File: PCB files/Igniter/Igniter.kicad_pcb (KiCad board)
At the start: 2 copper layers, 154.5 x 119.6 mm, 53 parts, among them IC1 74HC4050, J1 Micro_SD_Card, J2 Battery, J3 PT2, J4 PT1, J5 PT3, J6 PT4, J7 IgnitionCoil, Q1 N MOSFET, Q2 N MOSFET, Q3 N MOSFET, Q4 N MOSFET, Q5 N MOSFET, Q6 N MOSFET, U1 MIC3490, U2 FDS8984, U3 FDS8984, U4 FDS8984

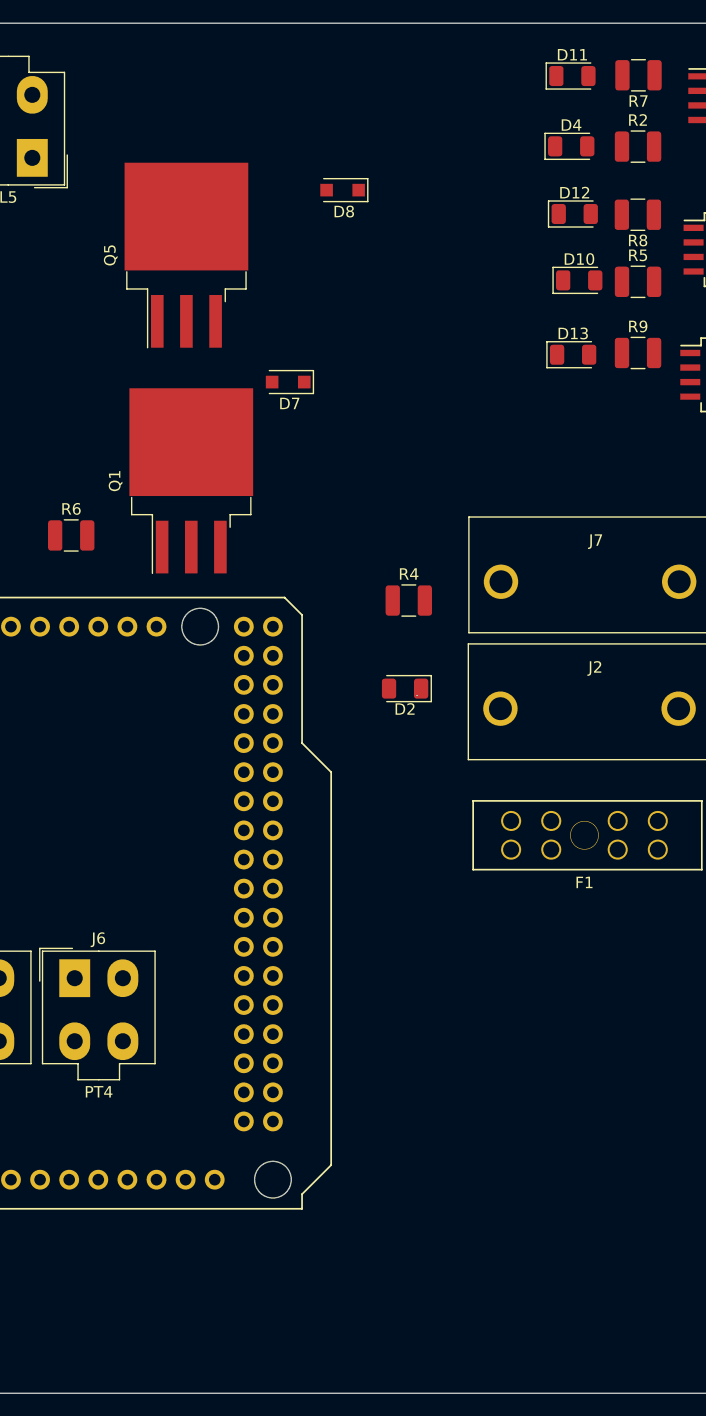
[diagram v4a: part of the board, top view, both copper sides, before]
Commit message: 11/14/2019
-Added a couple more mounting holes to keep board from flexing when plugging in connectors
-5V regulator likely not needed with new p ducers
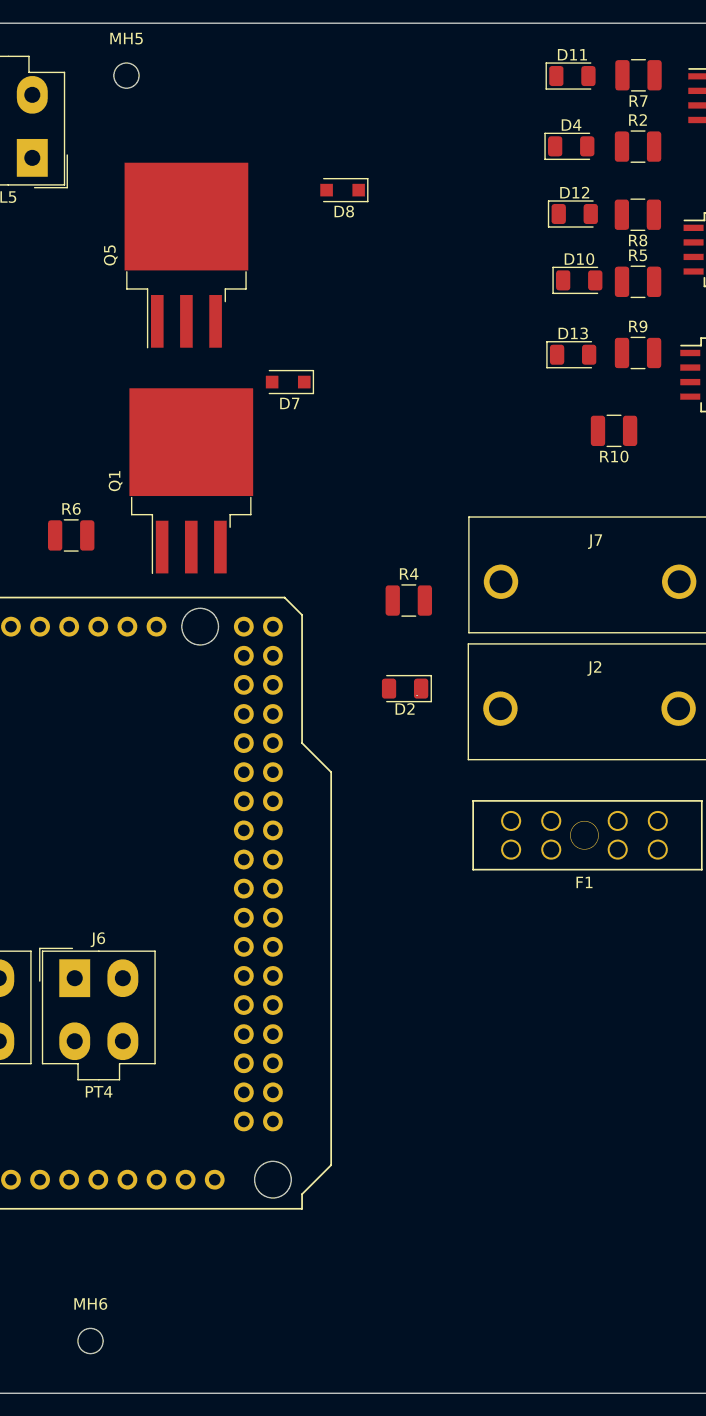
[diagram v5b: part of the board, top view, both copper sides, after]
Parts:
- added MH5: MountingHole, MountingHole:MountingHole_2.2mm_M2, F.Cu at (169.0, 40.7)
- added MH6: MountingHole, MountingHole:MountingHole_2.2mm_M2, F.Cu at (165.8, 151.2)
- added R10: 1k2, Resistor_SMD:R_1210_3225Metric, F.Cu at (211.5, 71.7)
- R2: value 1k2 -> 10k
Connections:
- R2 pad 1: Net-(D4-Pad2) -> PUSH1
- R2 pad 2: Net-(R2-Pad2) -> GNDREF
- R5 pad 1: Net-(D10-Pad2) -> Net-(D4-Pad2)
- R7 pad 1: Net-(R7-Pad1) -> Net-(D10-Pad2)
- R7 pad 2: Net-(D11-Pad2) -> Net-(R7-Pad2)
- R8 pad 2: Net-(D12-Pad2) -> Net-(D11-Pad2)
- R9 pad 2: Net-(D13-Pad2) -> Net-(D12-Pad2)
- U2 pad 1: Net-(R7-Pad1) -> Net-(R8-Pad1)
- U2 pad 3: Net-(R2-Pad2) -> Net-(R5-Pad2)
- U3 pad 1: Net-(R8-Pad1) -> Net-(R9-Pad1)
- U3 pad 3: Net-(R5-Pad2) -> Net-(R7-Pad2)
- U4 pad 1: Net-(R9-Pad1) -> Net-(R10-Pad1)
- XA1 pad D22: (no net) -> PUSH1

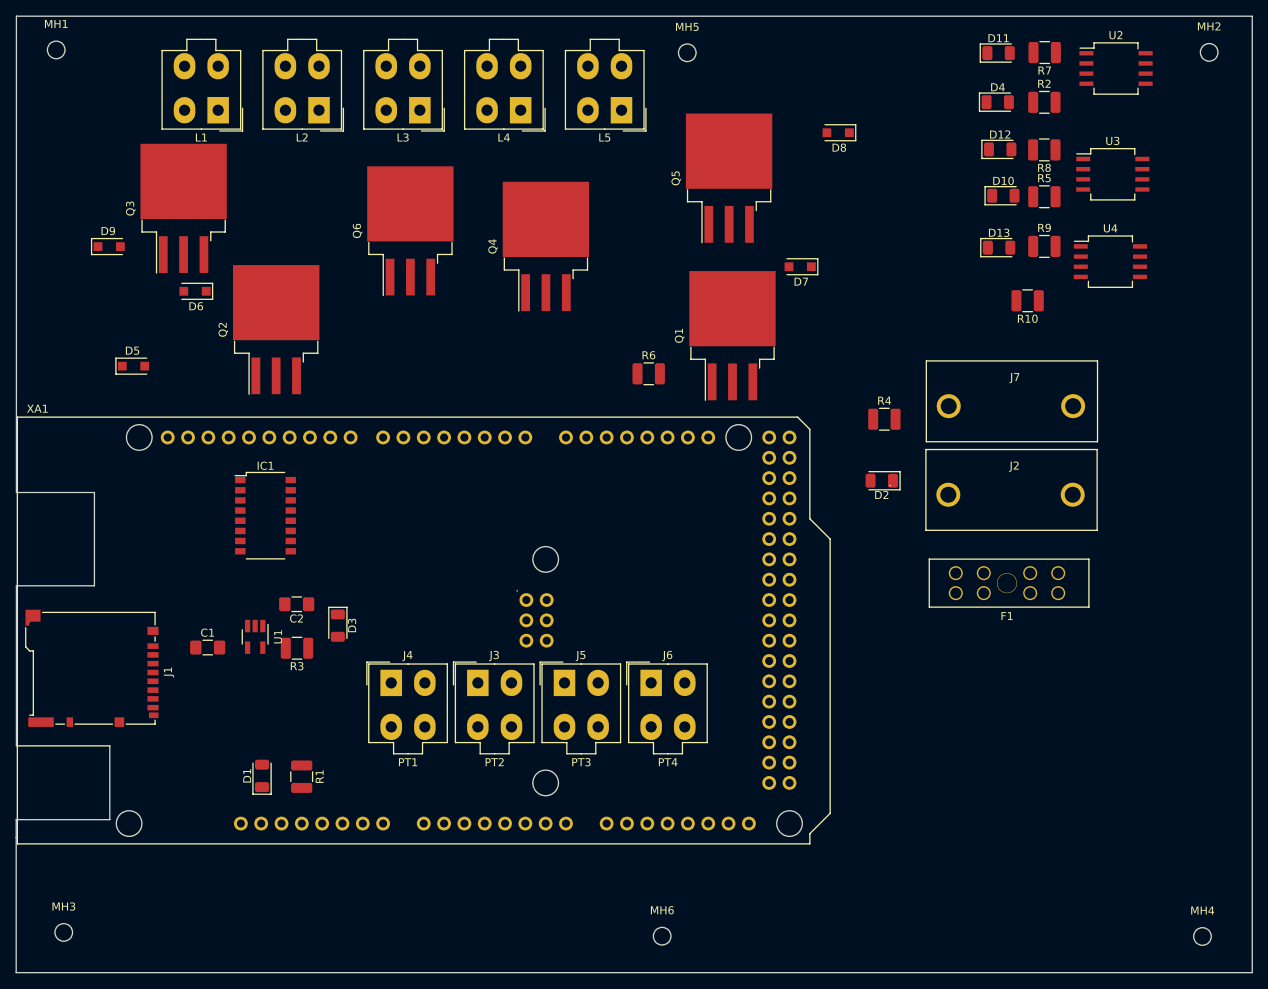
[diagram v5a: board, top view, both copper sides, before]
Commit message: 11/14/2019
-Removed 5V rail, no more 5V being used on this board
-Removed some global labels, replaced with wire connections or local net labels
-Added ignition coil primary flyback
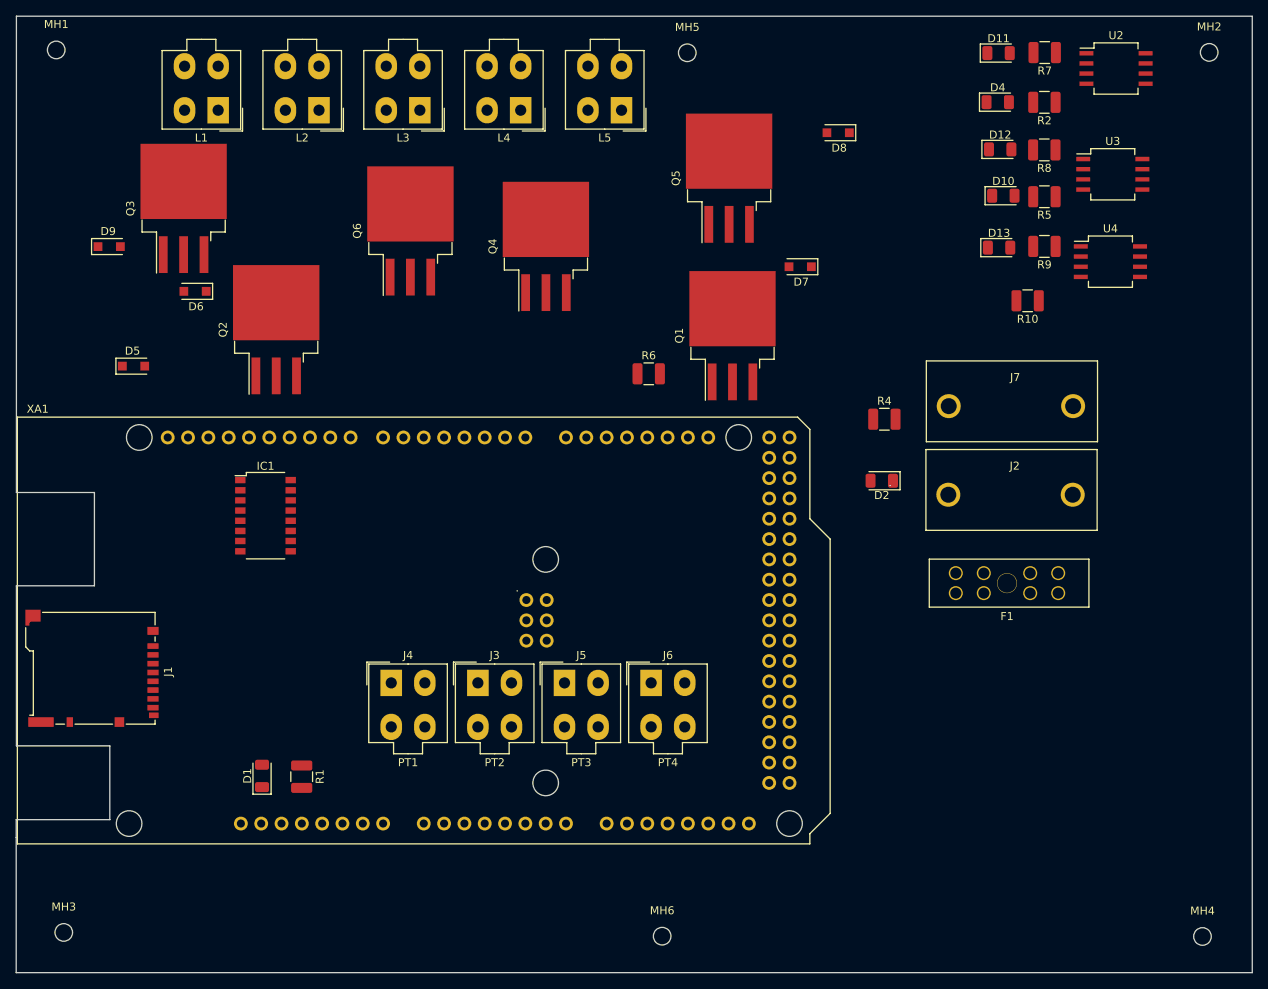
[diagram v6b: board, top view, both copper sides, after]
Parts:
- removed C1: 1u, Capacitor_SMD:C_1206_3216Metric_Pad1.42x1.75mm_HandSolder
- removed C2: 2.2u, Capacitor_SMD:C_1206_3216Metric_Pad1.42x1.75mm_HandSolder
- removed D3: 5V_GOOD, LED_SMD:LED_1206_3216Metric
- removed R3: 300, Resistor_SMD:R_1210_3225Metric
- removed U1: MIC3490, Package_TO_SOT_SMD:SOT-23-5_HandSoldering
- turned R2 to 180 degrees
- turned R5 to 180 degrees
- turned R9 to 180 degrees
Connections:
- net CLK renamed /SD/CLK
- net DI renamed /SD/DI
- net DO renamed /SD/DO
- net IGNITE renamed Net-(Q1-Pad1)
- net PT1 renamed /PT1

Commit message: 11/16/2019
-Selected smaller MOSFET SOT223
-Condensed PCB to a much smaller size
-Added Solenoid pulldowns
-Added all momentary switches
-Shrunk all resistors to 1206
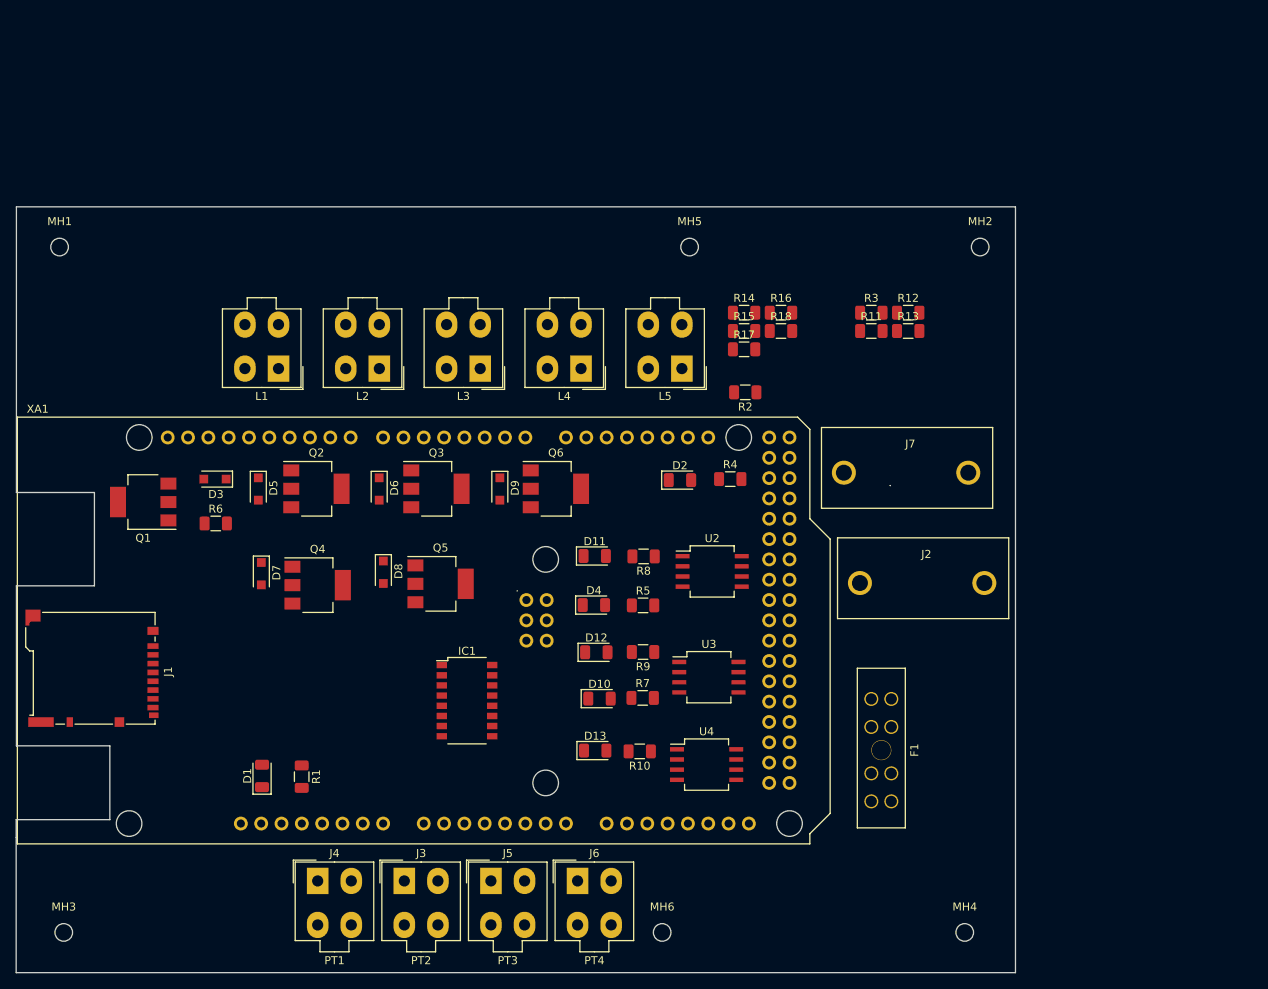
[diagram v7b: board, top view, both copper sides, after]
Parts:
- added D3: D_Small, Diode_SMD:D_SOD-123F, F.Cu at (109.9, 94.0)
- added R11: 10k, Resistor_SMD:R_1206_3216Metric, F.Cu at (192.0, 75.5)
- added R12: 10k, Resistor_SMD:R_1206_3216Metric, F.Cu at (196.6, 73.2)
- added R13: 10k, Resistor_SMD:R_1206_3216Metric, F.Cu at (196.6, 75.5)
- added R14: 10k, Resistor_SMD:R_1206_3216Metric, F.Cu at (176.1, 73.2)
- added R15: 10k, Resistor_SMD:R_1206_3216Metric, F.Cu at (176.1, 75.5)
- added R16: 10k, Resistor_SMD:R_1206_3216Metric, F.Cu at (180.7, 73.2)
- added R17: 10k, Resistor_SMD:R_1206_3216Metric, F.Cu at (176.1, 77.8)
- added R18: 10k, Resistor_SMD:R_1206_3216Metric, F.Cu at (180.7, 75.5)
- added R3: 10k, Resistor_SMD:R_1206_3216Metric, F.Cu at (192.0, 73.2)
- Q1, Q2, Q3, Q4, Q5, Q6: footprint Package_TO_SOT_SMD:TO-263-3_TabPin2 -> Package_TO_SOT_SMD:SOT-223
- R1, R10, R2, R4, R5, R6, R7, R8, R9: footprint Resistor_SMD:R_1210_3225Metric -> Resistor_SMD:R_1206_3216Metric
- moved R7 95.0 mm to (163.4, 121.4), turned to 0 degrees
- moved D11 80.6 mm to (157.4, 103.6)
- moved U3 80.6 mm to (171.7, 118.8)
- moved D10 80.6 mm to (158.0, 121.5)
- moved D13 80.6 mm to (157.5, 128.0)
- moved D4 80.6 mm to (157.3, 109.8)
- moved U2 80.6 mm to (172.1, 105.6)
- moved U4 80.6 mm to (171.4, 129.7)
- moved D12 80.6 mm to (157.6, 115.7)
- moved D8 79.1 mm to (131.0, 105.7), turned to 270 degrees
- moved D7 77.5 mm to (115.7, 105.9), turned to 270 degrees
- moved Q1 76.5 mm to (101.0, 96.9), turned to 180 degrees
- moved R10 74.3 mm to (163.0, 128.1)
- moved R5 71.6 mm to (163.4, 109.8), turned to 0 degrees
- moved R8 71.3 mm to (163.5, 103.7)
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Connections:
- net CS renamed /CS
- net PT2 renamed /PT2
- net PT3 renamed /PT3
- net PT4 renamed /PT4
- net PUSH1 renamed /PUSH1
- XA1 pad D23: (no net) -> /PUSH2
- XA1 pad D24: (no net) -> /PUSH3
- XA1 pad D25: (no net) -> /PUSH4
- XA1 pad D26: (no net) -> /PUSH5
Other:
- board size 154.5 x 119.6 mm -> 124.9 x 95.7 mm

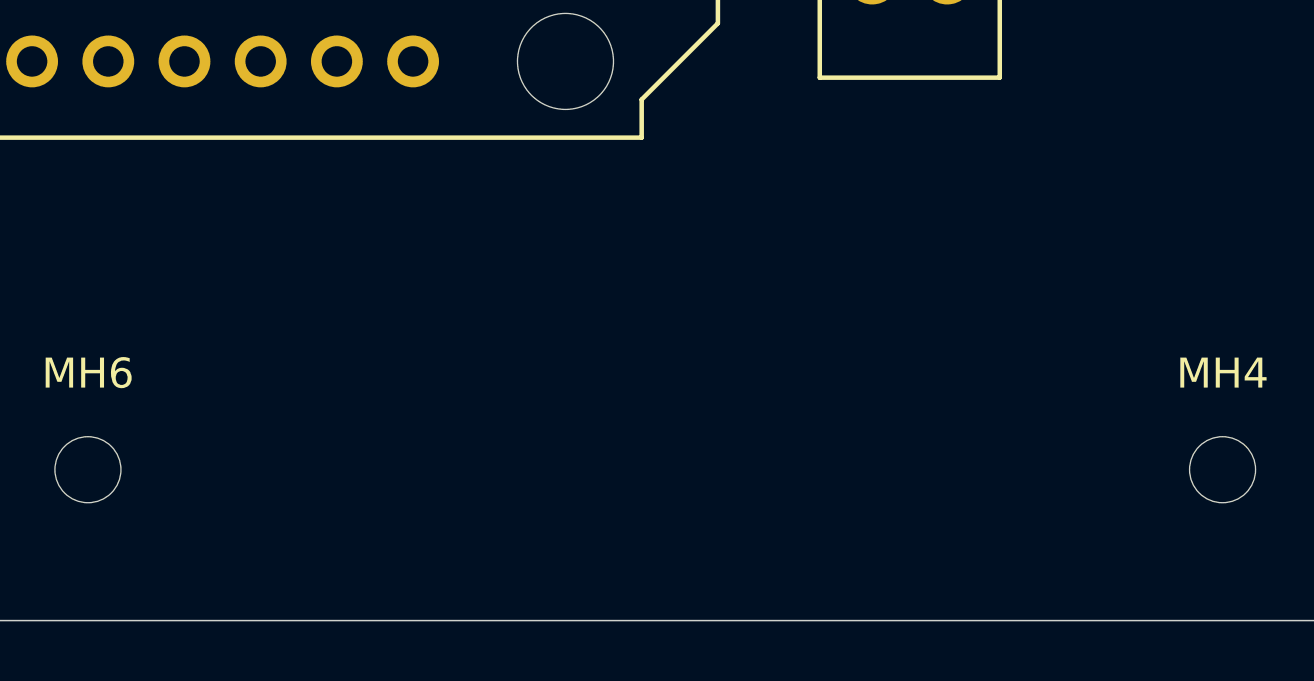
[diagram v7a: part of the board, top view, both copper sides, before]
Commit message: 11/16/2019
-Added rocket logo silkscreen
-Slight schematic visual changes
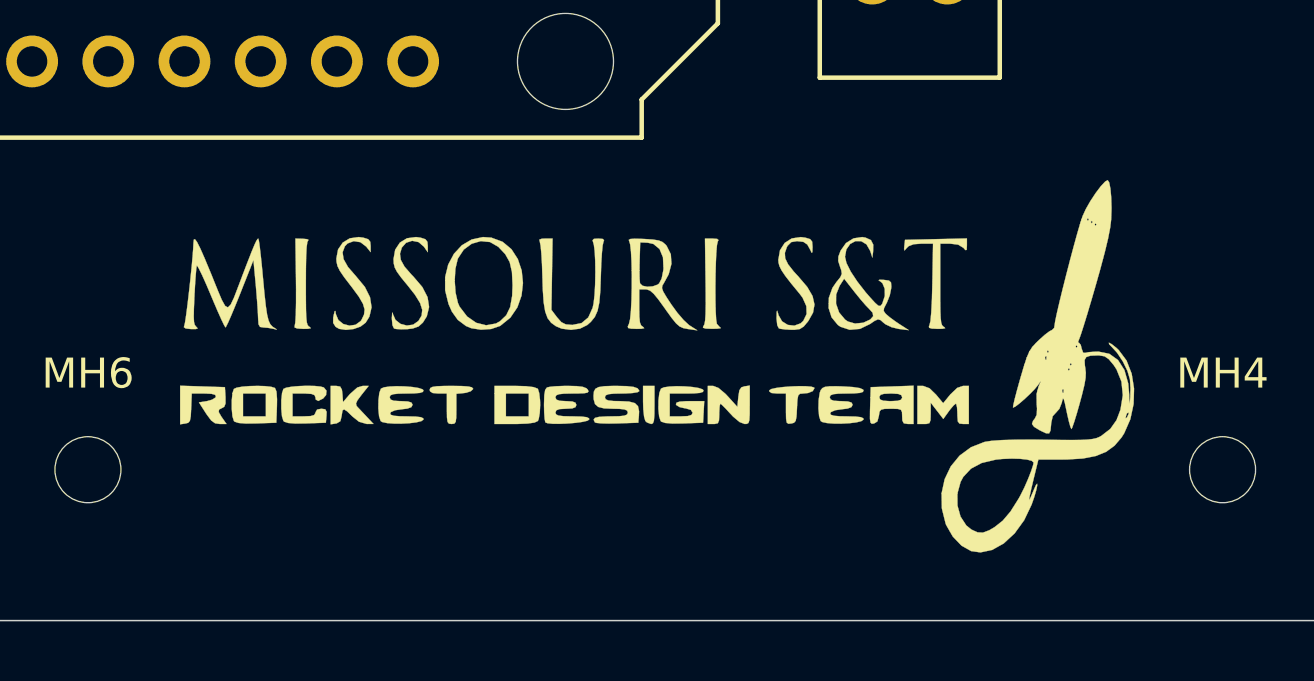
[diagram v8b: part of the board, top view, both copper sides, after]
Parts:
- added G***: LOGO, Board images:RocketLogo, F.Cu at (184.9, 147.4)
